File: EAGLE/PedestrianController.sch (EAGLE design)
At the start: 16 parts, among them CON1 FTDI, CON2 DS3231, CON3 AC110V, CON4 SIGNAL, IC1 ESP-WROOM-02

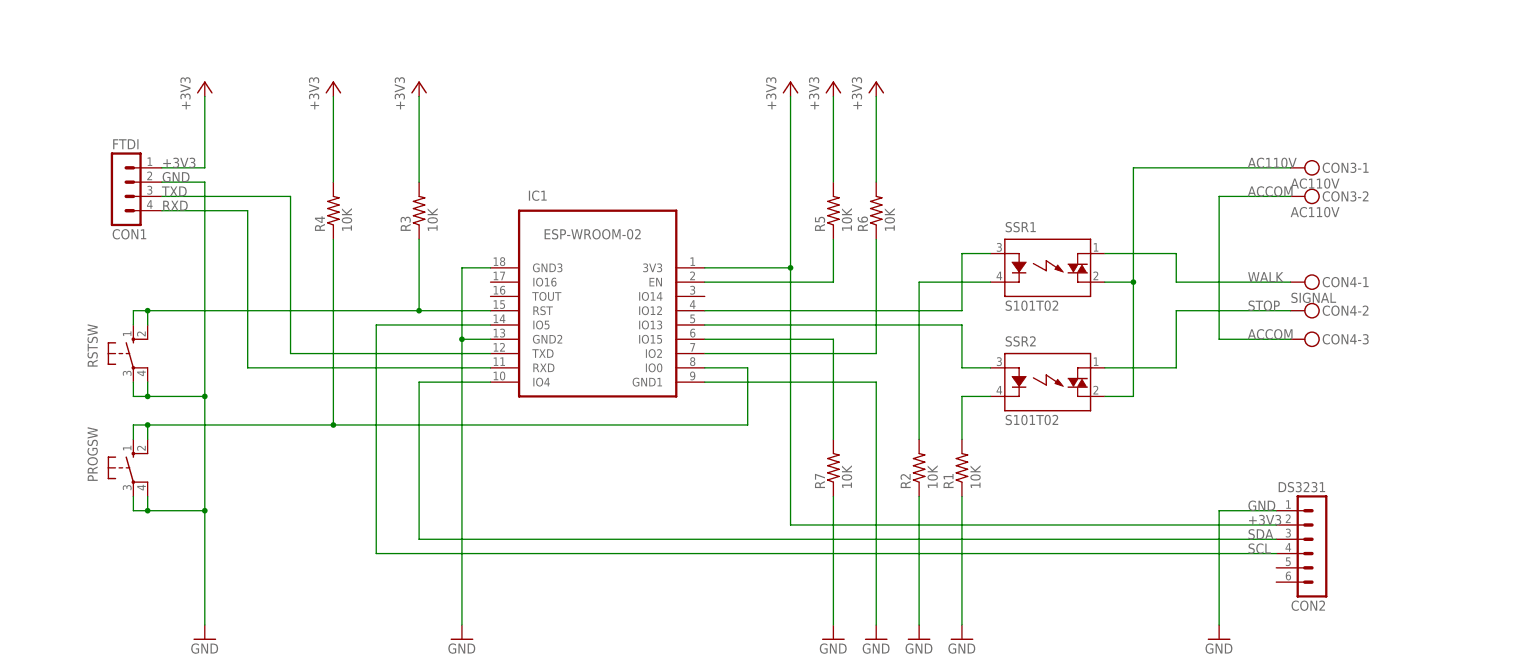
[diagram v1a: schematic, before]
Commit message: Rearrange parts, add leds.
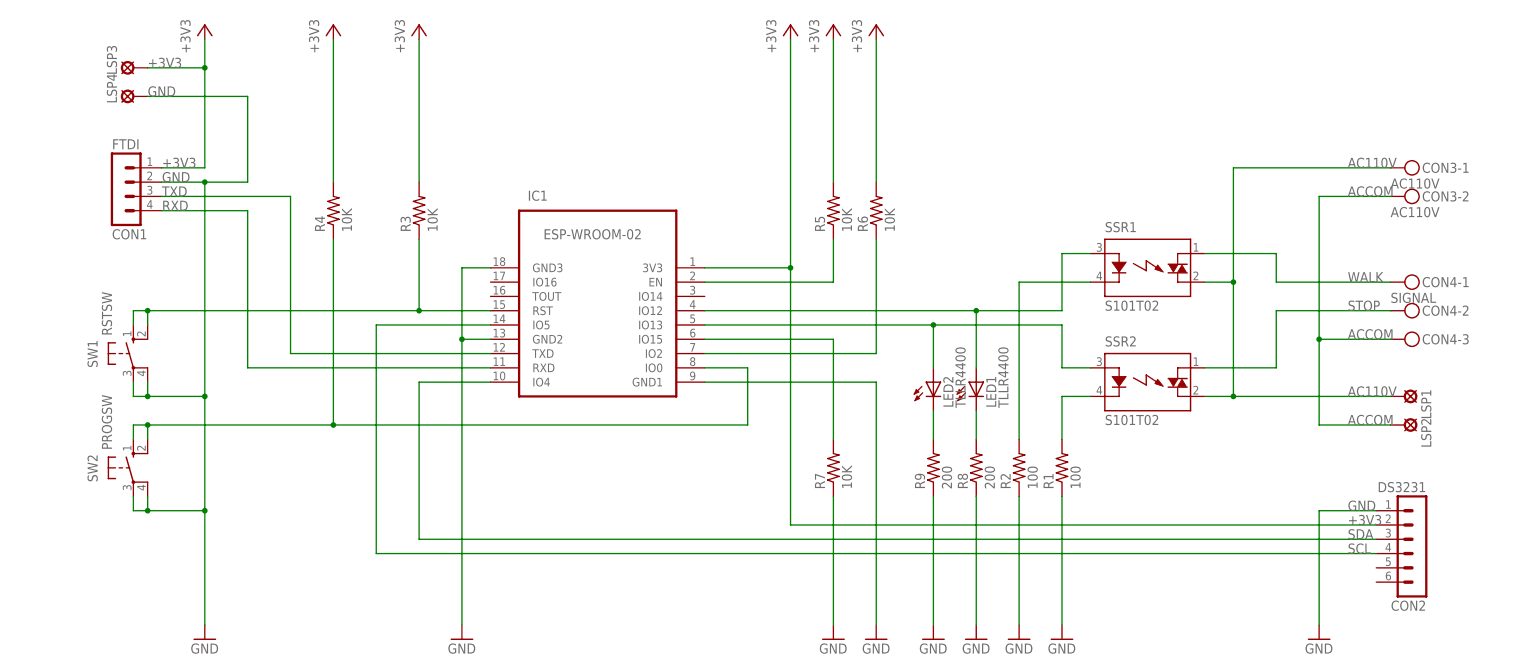
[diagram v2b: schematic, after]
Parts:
- added LED1, LED2: TLLR4400, PedestrianController:TLLR4400
- added LSP1, LSP2, LSP3, LSP4: LSP10, PedestrianController:LSP10
- added R8, R9: 200, PedestrianController:R-US_0204/7
- R1, R2: value 10K -> 100
- SW1: value (none) -> RSTSW
- SW2: value (none) -> PROGSW
- renumbered PROGSW to SW2, RSTSW to SW1
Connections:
- new net N$5: LED1.C, R8.2
- new net N$6: LED2.C, R9.2
- net +3V3: now also LSP3.MP
- net AC110V: now also LSP1.MP
- net ACCOM: now also LSP2.MP
- net GND: now also LSP4.MP, R8.1, R9.1
- net N$2: now also LED2.A
- net N$9: now also LED1.A
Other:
- moved on the sheet: CON2, CON3-1, CON3-2, CON4-1, CON4-2, CON4-3, R1, R2, SSR1, SSR2

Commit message: Add status LEDs.
* Improvement
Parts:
- added LED3: TLLR4400, PedestrianController:TLLR4400
- added R10: 200, PedestrianController:R-US_0204/7
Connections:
- new net N$11: LED3.C, R10.2
- new net N$8: IC1.IO14, LED3.A
- net GND: now also R10.1
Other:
- moved on the sheet: CON2, CON3-1, CON3-2, CON4-1, CON4-2, CON4-3, LED1, LED2, LSP1, LSP2, R1, R2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

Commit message: Rearrange wires.
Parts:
- added C1: 100u, PedestrianController:C-US050-024X044
- added C2: 0.1u, PedestrianController:C-US050-024X044
- R10, R8, R9: value 200 -> 510
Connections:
- net +3V3: now also C1.1, C2.1
- net GND: now also C1.2, C2.2
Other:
- moved on the sheet: CON1, LSP3, LSP4, SW1, SW2

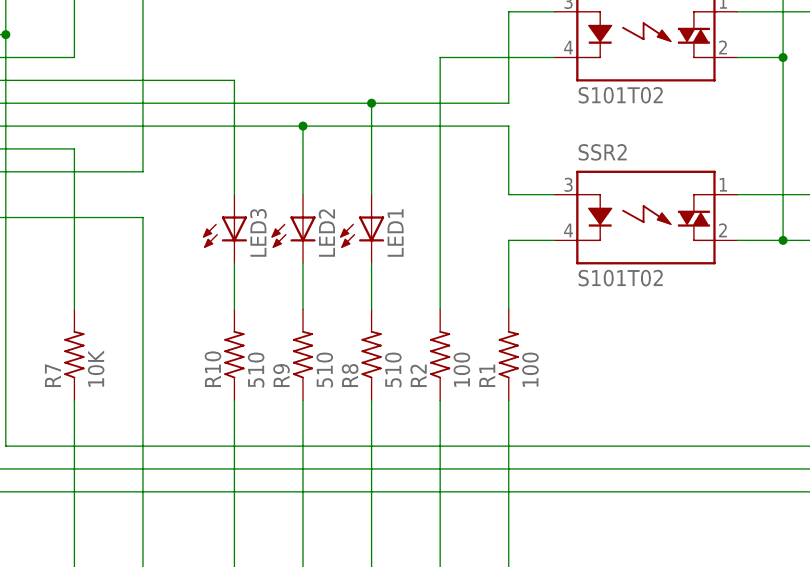
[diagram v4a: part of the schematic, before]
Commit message: Adjust resistor values by GPIO current specs.
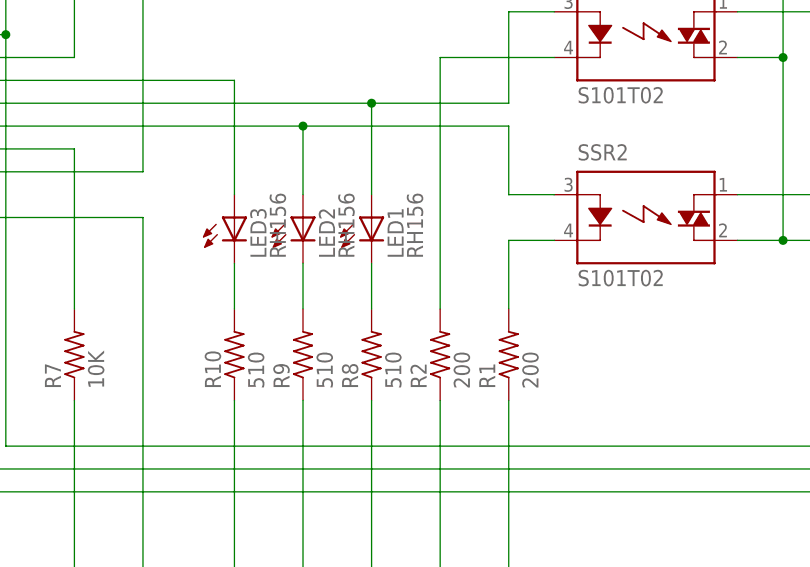
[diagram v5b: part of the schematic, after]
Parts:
- LED1, LED2, LED3: value TLLR4400 -> RH156
- R1, R2: value 100 -> 200
- R10: SPICEPREFIX (none) -> R
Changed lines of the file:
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@@
 <part name="SSR2" library="PedestrianController" deviceset="S?*" device="101T" package3d_urn="urn:adsk.eagle:package:24508/1" technology="02"/>
 <part name="SSR1" library="PedestrianController" deviceset="S?*" device="101T" package3d_urn="urn:adsk.eagle:package:24508/1" technology="02"/>
-<part name="R1" library="PedestrianController" deviceset="R-US_" device="0204/7" package3d_urn="urn:adsk.eagle:package:25945/1" value="100"/>
-<part name="R2" library="PedestrianController" deviceset="R-US_" device="0204/7" package3d_urn="urn:adsk.eagle:package:25945/1" value="100"/>
+<part name="R1" library="PedestrianController" deviceset="R-US_" device="0204/7" package3d_urn="urn:adsk.eagle:package:25945/1" value="200"/>
+<part name="R2" library="PedestrianController" deviceset="R-US_" device="0204/7" package3d_urn="urn:adsk.eagle:package:25945/1" value="200"/>
 <part name="R3" library="PedestrianController" deviceset="R-US_" device="0204/7" package3d_urn="urn:adsk.eagle:package:25945/1" value="10K"/>
 <part name="R4" library="PedestrianController" deviceset="R-US_" device="0204/7" package3d_urn="urn:adsk.eagle:package:25945/1" value="10K"/>
@@
 <part name="GND8" library="PedestrianController" deviceset="GND" device=""/>
 <part name="GND9" library="PedestrianController" deviceset="GND" device=""/>
-<part name="LED1" library="PedestrianController" deviceset="TLLR4400" device="" package3d_urn="urn:adsk.eagle:package:15797/1" value=""/>
-<part name="LED2" library="PedestrianController" deviceset="TLLR4400" device="" package3d_urn="urn:adsk.eagle:package:15797/1" value=""/>
-<part name="R10" library="PedestrianController" deviceset="R-US_" device="0204/7" package3d_urn="urn:adsk.eagle:package:25945/1" value="510"/>
+<part name="LED1" library="PedestrianController" deviceset="TLLR4400" device="" package3d_urn="urn:adsk.eagle:package:15797/1" value="RH156"/>
+<part name="LED2" library="PedestrianController" deviceset="TLLR4400" device="" package3d_urn="urn:adsk.eagle:package:15797/1" value="RH156"/>
+<part name="R10" library="PedestrianController" deviceset="R-US_" device="0204/7" package3d_urn="urn:adsk.eagle:package:25945/1" value="510">
+<attribute name="SPICEPREFIX" value="R"/>
+</part>
 <part name="GND11" library="PedestrianController" deviceset="GND" device=""/>
-<part name="LED3" library="PedestrianController" deviceset="TLLR4400" device="" package3d_urn="urn:adsk.eagle:package:15797/1" value=""/>
+<part name="LED3" library="PedestrianController" deviceset="TLLR4400" device="" package3d_urn="urn:adsk.eagle:package:15797/1" value="RH156"/>
 <part name="C1" library="PedestrianController" deviceset="C-US" device="050-024X044" package3d_urn="urn:adsk.eagle:package:26162/1" value="100u"/>
 <part name="C2" library="PedestrianController" deviceset="C-US" device="050-024X044" package3d_urn="urn:adsk.eagle:package:26162/1" value="0.1u"/>
